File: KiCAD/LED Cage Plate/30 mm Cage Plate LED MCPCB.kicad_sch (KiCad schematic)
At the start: 29 parts, among them IC1 AL8843QSP-13, J1 Conn_01x08_Socket, J2 0, M1 Fan, Q5 2x_p-channel, Q6 2x_p-channel

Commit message: Working draft of driver circuit
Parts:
- removed M1: Fan, symbol Motor:Fan
- added M2: Fan_4pin, symbol Motor:Fan_4pin
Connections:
- net GND: now also M2.1 (-)
- net PWM: now also M2.4 (PWM)
- net Vin: now also M2.2 (+)
- no-connect marks 0 -> 1
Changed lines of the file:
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@@
 		(color 0 0 0 0)
 	)
+	(no_connect
+		(at 87.63 120.65)
+	)
 	(wire
 		(pts
@@
 	(wire
 		(pts
+			(xy 86.36 125.73) (xy 87.63 125.73)
+		)
+		(stroke
+			(width 0)
+			(type default)
+		)
+	)
+	(wire
+		(pts
 			(xy 153.67 39.37) (xy 158.75 39.37)
 		)
@@
 		)
 	)
+	(label "PWM"
+		(at 86.36 125.73 180)
+		(fields_autoplaced yes)
+		(effects
+			(font
+				(size 1.27 1.27)
+			)
+			(justify right bottom)
+		)
+	)
 	(label "LED+"
 		(at 170.18 26.67 0)
@@
 	)
 	(symbol
+		(lib_id "Motor:Fan_4pin")
+		(at 95.25 123.19 0)
+		(unit 1)
+		(exclude_from_sim no)
+		(in_bom yes)
+		(on_board no)
+		(dnp no)
+		(fields_autoplaced yes)
+		(property "Reference" "M2"
+			(at 99.2632 121.9778 0)
+			(effects
+				(font
+					(size 1.27 1.27)
+				)
+				(justify left)
+			)
+		)
+		(property "Value" "Fan_4pin"
+			(at 99.2632 124.4021 0)
+			(effects
+				(font
+					(size 1.27 1.27)
+				)
+				(justify left)
+			)
+		)
+		(property "Footprint" ""
+			(at 95.25 122.936 0)
+			(effects
+				(font
+					(size 1.27 1.27)
+				)
+				(hide yes)
+			)
+		)
+		(property "Datasheet" "https://wakefieldthermal.com/content/data_sheets/wfv-dc-fans-rev-a3%20%281%29.pdf"
+			(at 95.25 122.936 0)
+			(effects
+				(font
+					(size 1.27 1.27)
+				)
+				(hide yes)
+			)
+		)
+		(property "Description" "FAN AXIAL 35X10MM 12VDC WIRE"
+			(at 95.25 123.19 0)
+			(effects
+				(font
+					(size 1.27 1.27)
+				)
+				(hide yes)
+			)
+		)
+		(property "Manufacturer" "Wakefield-Vette"
+			(at 95.25 123.19 0)
+			(effects
+				(font
+					(size 1.27 1.27)
+				)
+				(hide yes)
+			)
+		)
+		(property "Part" "DC0351012W2B-BT0"
+			(at 95.25 123.19 0)
+			(effects
+				(font
+					(size 1.27 1.27)
+				)
+				(hide yes)
+			)
+		)
+		(pin "1"
+		)
+		(pin "4"
+		)
+		(pin "3"
+		)
+		(pin "2"
+		)
+		(instances
+			(project ""
+				(path "/d4bfa918-6f2d-41e7-978b-b2160bded453"
+					(reference "M2")
+					(unit 1)
+				)
+			)
+		)
+	)
+	(symbol
 		(lib_id "Device:C_Small")
 		(at 194.31 109.22 180)
@@
 					(unit 1)
 				)
-			)
-		)
-	)
-	(symbol
-		(lib_id "Motor:Fan")
-		(at 95.25 123.19 0)
-		(unit 1)
-		(exclude_from_sim no)
-		(in_bom yes)
-		(on_board yes)
-		(dnp no)
-		(fields_autoplaced yes)
-		(property "Reference" "M1"
-			(at 99.2632 121.9778 0)
-			(effects
-				(font
-					(size 1.27 1.27)
-				)
-				(justify left)
-			)
-		)
-		(property "Value" "Fan"
-			(at 99.2632 124.4021 0)
-			(effects
-				(font
-					(size 1.27 1.27)
-				)
-				(justify left)
-			)
-		)
-		(property "Footprint" ""
-			(at 95.25 122.936 0)
-			(effects
-				(font
-					(size 1.27 1.27)
-				)
-				(hide yes)
-			)
-		)
-		(property "Datasheet" "https://www.sunon.com/PROSEARCH_FILES/(D03033640G-01)-1.pdf"
-			(at 95.25 122.936 0)
-			(effects
-				(font
-					(size 1.27 1.27)
-				)
-				(hide yes)
-			)
-		)
-		(property "Description" "Fan"
-			(at 95.25 123.19 0)
-			(effects
-				(font
-					(size 1.27 1.27)
-				)
-				(hide yes)
-			)
-		)
-		(property "Manufacturer" "Sunon Fans"
-			(at 95.25 123.19 0)
-			(effects
-				(font
-					(size 1.27 1.27)
-				)
-				(hide yes)
-			)
-		)
-		(property "Part" "HA30101V3-1000U-A99"
-			(at 95.25 123.19 0)
-			(effects
-				(font
-					(size 1.27 1.27)
-				)
-				(hide yes)
-			)
-		)
-		(pin "2"
-		)
-		(pin "1"
-		)
-		(instances
-			(project ""
-				(path "/d4bfa918-6f2d-41e7-978b-b2160bded453"
-					(reference "M1")
-					(unit 1)
-				)

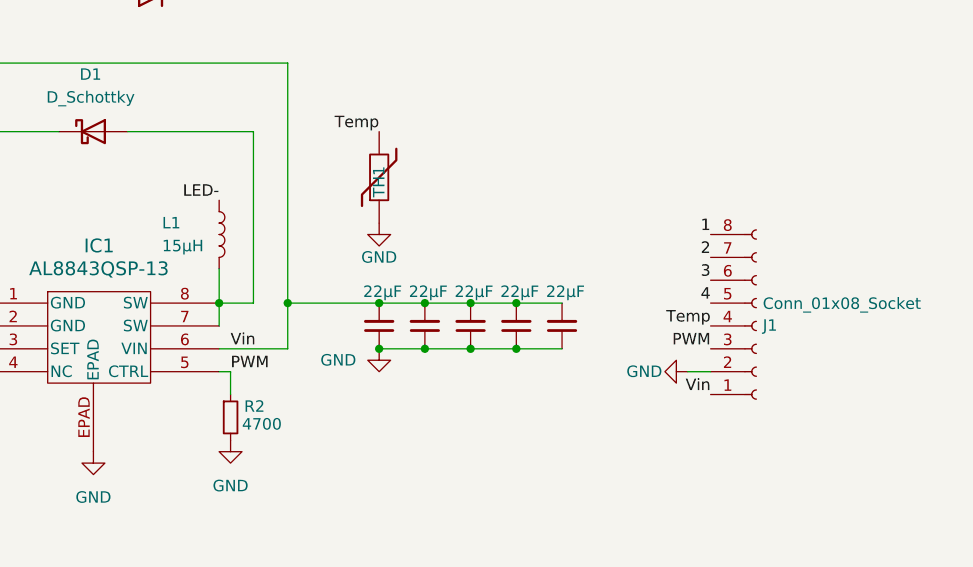
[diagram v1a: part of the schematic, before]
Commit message: Improve clearance of gate traces on LED plate
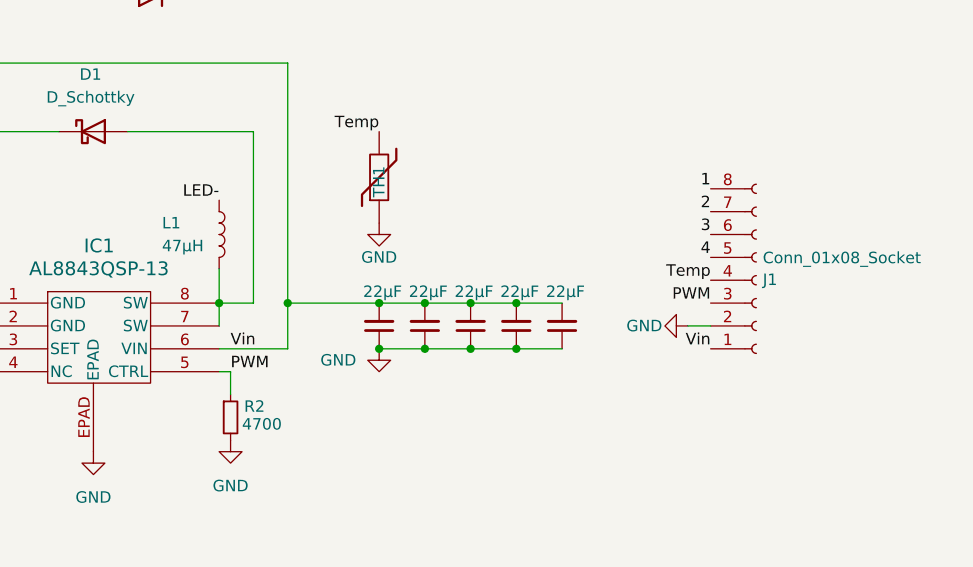
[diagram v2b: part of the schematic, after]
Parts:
- L1: value 15μH -> 47μH; Part SRP1038A-150M -> SRP1038AA-470M
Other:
- moved on the sheet: J1
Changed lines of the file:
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@@
 	(wire
 		(pts
-			(xy 208.28 114.3) (xy 210.82 114.3)
+			(xy 208.28 109.22) (xy 210.82 109.22)
 		)
 		(stroke
@@
 	)
 	(label "Vin"
-		(at 210.82 116.84 180)
+		(at 210.82 111.76 180)
 		(fields_autoplaced yes)
 		(effects
@@
 	)
 	(label "3"
-		(at 210.82 104.14 180)
+		(at 210.82 99.06 180)
 		(fields_autoplaced yes)
 		(effects
@@
 	)
 	(label "1"
-		(at 210.82 99.06 180)
+		(at 210.82 93.98 180)
 		(fields_autoplaced yes)
 		(effects
@@
 	)
 	(label "2"
-		(at 210.82 101.6 180)
+		(at 210.82 96.52 180)
 		(fields_autoplaced yes)
 		(effects
@@
 	)
 	(label "Temp"
-		(at 210.82 109.22 180)
+		(at 210.82 104.14 180)
 		(fields_autoplaced yes)
 		(effects
@@
 	)
 	(label "PWM"
-		(at 210.82 111.76 180)
+		(at 210.82 106.68 180)
 		(fields_autoplaced yes)
 		(effects
@@
 	)
 	(label "4"
-		(at 210.82 106.68 180)
+		(at 210.82 101.6 180)
 		(fields_autoplaced yes)
 		(effects
@@
 	(symbol
 		(lib_id "Connector:Conn_01x08_Socket")
-		(at 215.9 109.22 0)
+		(at 215.9 104.14 0)
 		(mirror x)
 		(unit 1)
@@
 		(dnp no)
 		(property "Reference" "J1"
-			(at 216.6112 109.1622 0)
+			(at 216.6112 104.0822 0)
 			(effects
 				(font
@@
 		)
 		(property "Value" "Conn_01x08_Socket"
-			(at 216.6112 106.7379 0)
+			(at 216.6112 101.6579 0)
 			(effects
 				(font
@@
 		)
 		(property "Footprint" "Custom:SAMTEC_SSM-108-F-SH-TR"
-			(at 215.9 109.22 0)
+			(at 215.9 104.14 0)
 			(effects
 				(font
@@
 		)
 		(property "Datasheet" "https://mm.digikey.com/Volume0/opasdata/d220001/medias/docus/6129/ssm-1xx-xxx-xx-xx-xx-xx-x-xx-mkt.pdf"
-			(at 215.9 109.22 0)
+			(at 215.9 104.14 0)
 			(effects
 				(font
@@
 		)
 		(property "Description" "Generic connector, single row, 01x08, script generated"
-			(at 215.9 109.22 0)
+			(at 215.9 104.14 0)
 			(effects
 				(font
@@
 		)
 		(property "Manufacturer" "Samtec Inc."
-			(at 215.9 109.22 0)
+			(at 215.9 104.14 0)
 			(effects
 				(font
@@
 		)
 		(property "Part" "SSM-108-F-SH-TR"
-			(at 215.9 109.22 0)
+			(at 215.9 104.14 0)
 			(effects
 				(font
@@
 			)
 		)
-		(property "Datasheet" "https://www.gofordsemi.com/upload/cn/propdf/G220P03S2.pdf"
+		(property "Datasheet" "https://www.gofordsemi.com/upload/cn/propdf/G200P04S2.pdf"
 			(at 139.7 41.8846 0)
 			(effects
@@
 			)
 		)
-		(property "Value" "15μH"
+		(property "Value" "47μH"
 			(at 149.86 100.33 0)
 			(effects
@@
 			)
 		)
-		(property "Description" ""
+		(property "Description" "IND,11X10X3.8MM,47UH20%,3.5A,SHD"
 			(at 156.21 99.06 0)
 			(effects
@@
 			)
 		)
-		(property "Part" "SRP1038A-150M"
+		(property "Part" "SRP1038AA-470M"
 			(at 156.21 99.06 0)
 			(effects
@@
 	(symbol
 		(lib_id "power:GND")
-		(at 208.28 114.3 270)
+		(at 208.28 109.22 270)
 		(unit 1)
 		(exclude_from_sim no)
@@
 		(dnp no)
 		(property "Reference" "#PWR04"
-			(at 201.93 114.3 0)
+			(at 201.93 109.22 0)
 			(effects
 				(font
@@
 		)
 		(property "Value" "GND"
-			(at 203.454 114.3 90)
+			(at 203.454 109.22 90)
 			(effects
 				(font
@@
 		)
 		(property "Footprint" ""
-			(at 208.28 114.3 0)
+			(at 208.28 109.22 0)
 			(effects
 				(font
@@
 		)
 		(property "Datasheet" ""
-			(at 208.28 114.3 0)
+			(at 208.28 109.22 0)
 			(effects
 				(font
@@
 		)
 		(property "Description" ""
-			(at 208.28 114.3 0)
-			(effects
-				(font
+			(at 208.28 109.22 0)
+			(effects
+				(font

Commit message: Ordered version
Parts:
- added H5, H6, H7, H8: MountingHole, symbol Mechanical:MountingHole
- added J3: RJ45_Shielded, symbol Connector:RJ45_Shielded
- added J4: Conn_01x08_Pin, symbol Connector:Conn_01x08_Pin
- H1, H2, H3, H4: now left out of the parts list
- J1: Part SSM-108-F-SH-TR -> SSM-108-L-SH-TR
- J2: Part 5104 -> 5108
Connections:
- net 1: now also J3.8, J4.8 (Pin_8)
- net 2: now also J3.7, J4.7 (Pin_7)
- net 3: now also J3.6, J4.6 (Pin_6)
- net 4: now also J3.5, J4.5 (Pin_5)
- net GND: now also J3.2, J3.SH, J4.2 (Pin_2)
- net PWM: now also J3.3, J4.3 (Pin_3)
- net Temp: now also J3.4, J4.4 (Pin_4)
- net Vin: now also J3.1, J4.1 (Pin_1)
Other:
- note added: "Cable Assembly"
- note added: "Drill fan holes to 4 mm"
- note added: "Fan Mounting Bolts"

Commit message: Working draft of series LED - passes DRC
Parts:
- removed D2: D_Zener, Custom:DFN6_TDS3011_SEM, symbol Device:D_Zener
- removed J2: 0, Resistor_SMD:R_1206_3216Metric, symbol Device:R
- removed Q5, Q6: 2x_p-channel, Custom:SOP-8_3.9x4.9mm_P1.27mm, symbol LED Driver 1x8 Mux-rescue:IRF9358TRPBF-2x_p-channel-Custom_parts
- removed RN1: 4700, Resistor_SMD:R_Array_Convex_4x1206, symbol Device:R_Pack04
- added D11: D_Zener, Custom:DFN6_TDS3011_SEM, symbol Device:D_Zener
- added Q1: Q_PMOS, Custom:SON8_DMP4025SFGQ-13_DIO, symbol Device:Q_PMOS_SGD
- added Q2: Q_NMOS, Package_TO_SOT_SMD:SOT-23, symbol Device:Q_NMOS_GSD
- added R3: 10k, Resistor_SMD:R_0603_1608Metric, symbol Device:R_Small
- R2: value 4700 -> 10k; Manufacturer Stackpole Electronics Inc -> Vishay Dale; Part RMCF0603FT4K70 -> RCA060310K0FKEAHP
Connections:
- net 1 is gone; now on net GND: J1.8 (Pin_8), J3.8, J4.8 (Pin_8)
- net 3 is gone; now on net GND: J1.6 (Pin_6), J3.6, J4.6 (Pin_6)
- net 4 is gone; now on net Temp: J1.5 (Pin_5), J3.5, J4.5 (Pin_5)
- net GND: now also J1.4 (Pin_4), J3.4, J4.4 (Pin_4), Q2.2 (S), R3.2; no longer R2.2
- net LED+: now also R2.1, D11.1 (K), Q1.1 (S); no longer D3.2 (A), D3.3 (PAD), D4.2 (A), D4.3 (PAD), D5.2 (A), D5.3 (PAD), D6.2 (A), D6.3 (PAD)
- net LED-: now also D6.1 (K), D11.2 (A)
- net PWM: no longer R2.1
- net Temp: no longer J1.4 (Pin_4), J3.4, J4.4 (Pin_4)
- net at D3.1 (K): now also D4.2 (A)
- net at D4.1 (K): now also D5.2 (A)
- net at D5.1 (K): now also D6.2 (A)
- net 2 renamed Gate
- net Gate: now also Q2.1 (G), R3.1
- new net: Q1.2 (G), Q2.3 (D), R2.2
- new net: D3.2 (A), D3.3 (PAD), D4.3 (PAD), D5.3 (PAD), D6.3 (PAD), Q1.3 (D)
